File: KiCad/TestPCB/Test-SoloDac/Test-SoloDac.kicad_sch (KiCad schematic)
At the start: 26 parts, among them J1 Conn_01x01_Male, J2 Conn_01x01_Male, U1 TL431D

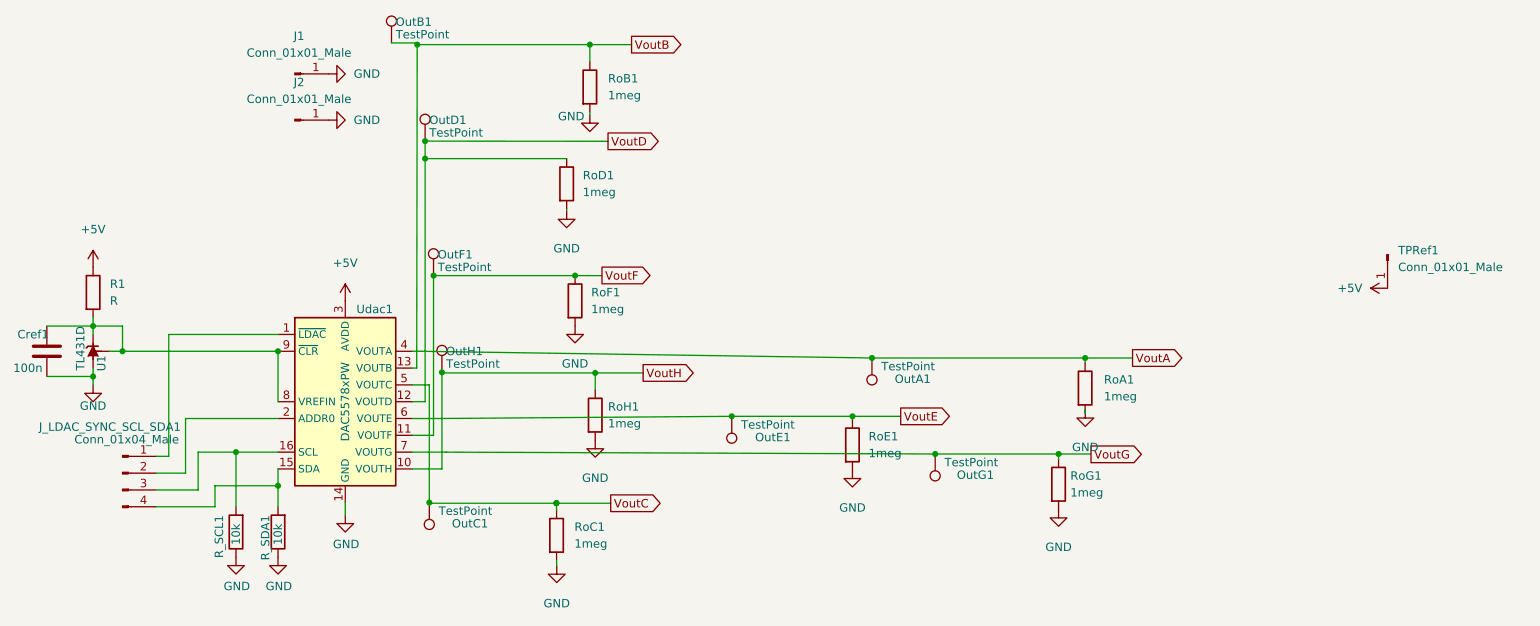
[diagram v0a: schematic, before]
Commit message: Removidos los pads. Agregados pines y jumpers
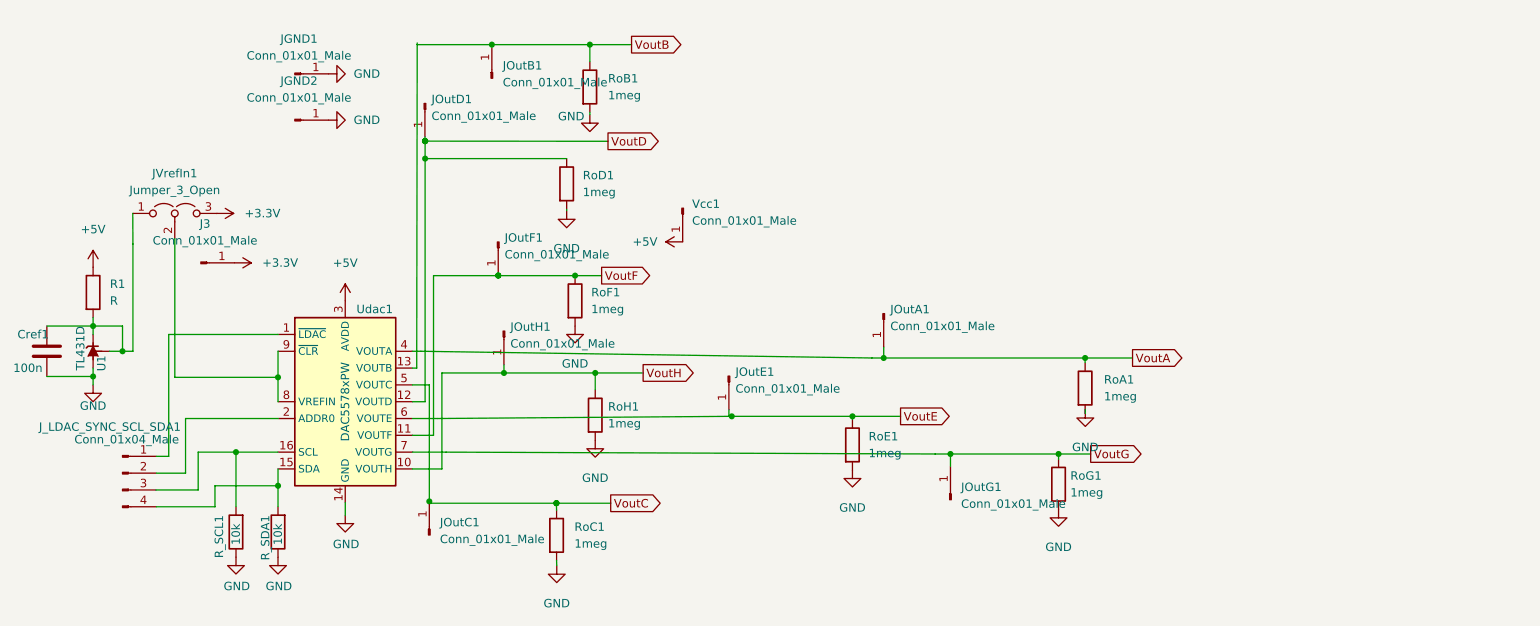
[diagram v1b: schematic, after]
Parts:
- removed OutA1, OutB1, OutC1, OutD1, OutE1, OutF1, OutG1, OutH1: TestPoint, TestPoint:TestPoint_Pad_4.0x4.0mm, symbol Connector:TestPoint
- added J3, JOutA1, JOutB1, JOutC1, JOutD1, JOutE1, JOutF1, JOutG1, JOutH1: Conn_01x01_Male, Connector_PinHeader_2.54mm:PinHeader_1x01_P2.54mm_Vertical, symbol Connector:Conn_01x01_Male
- added JVrefIn1: Jumper_3_Open, Connector_PinHeader_2.54mm:PinHeader_1x03_P2.54mm_Vertical, symbol Jumper:Jumper_3_Open
- JGND1: renamed from J1; footprint Connector_PinHeader_2.00mm:PinHeader_1x01_P2.00mm_Vertical -> Connector_PinHeader_2.54mm:PinHeader_1x01_P2.54mm_Vertical
- JGND2: renamed from J2; footprint Connector_PinHeader_2.00mm:PinHeader_1x01_P2.00mm_Vertical -> Connector_PinHeader_2.54mm:PinHeader_1x01_P2.54mm_Vertical
- J_LDAC_SYNC_SCL_SDA1: footprint Connector_PinHeader_2.00mm:PinHeader_1x04_P2.00mm_Vertical -> Connector_PinHeader_2.54mm:PinHeader_1x04_P2.54mm_Vertical
- renumbered TPRef1 to Vcc1
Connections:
- net VoutA: now also JOutA1.1 (Pin_1)
- net VoutB: now also JOutB1.1 (Pin_1)
- net VoutC: now also JOutC1.1 (Pin_1)
- net VoutD: now also JOutD1.1 (Pin_1)
- net VoutE: now also RoE1.1, Udac1.6 (VOUTE), JOutE1.1 (Pin_1)
- net VoutF: now also RoF1.1, Udac1.11 (VOUTF), JOutF1.1 (Pin_1)
- net VoutG: now also RoG1.1, Udac1.7 (VOUTG), JOutG1.1 (Pin_1)
- net VoutH: now also JOutH1.1 (Pin_1)
- net at Cref1.1, R1.2, U1.1 (K)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: now also JVrefIn1.1 (A); no longer Udac1.8 (VREFIN), Udac1.9 (~{CLR})
- new net: JVrefIn1.2 (C), Udac1.8 (VREFIN), Udac1.9 (~{CLR})
- new net +3V3: J3.1 (Pin_1), JVrefIn1.3 (B)
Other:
- moved on the sheet: Vcc1
